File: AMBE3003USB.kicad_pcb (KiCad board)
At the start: 2 copper layers, 95 x 85 mm, 208 parts, among them J1 McBSP, J2 USB_OTG, J4 CODEC, P1 GND, P2 Config, P3 3v3, P4 VSET, P5 HARD RESET, P6 SEQ, P7 3v3, P8 ACONF, P9 GND, Q1 BC847, U1 AMBE3003, U2 TPS75005RGW_wPin21, U3 FT232RL, X1 29.4912

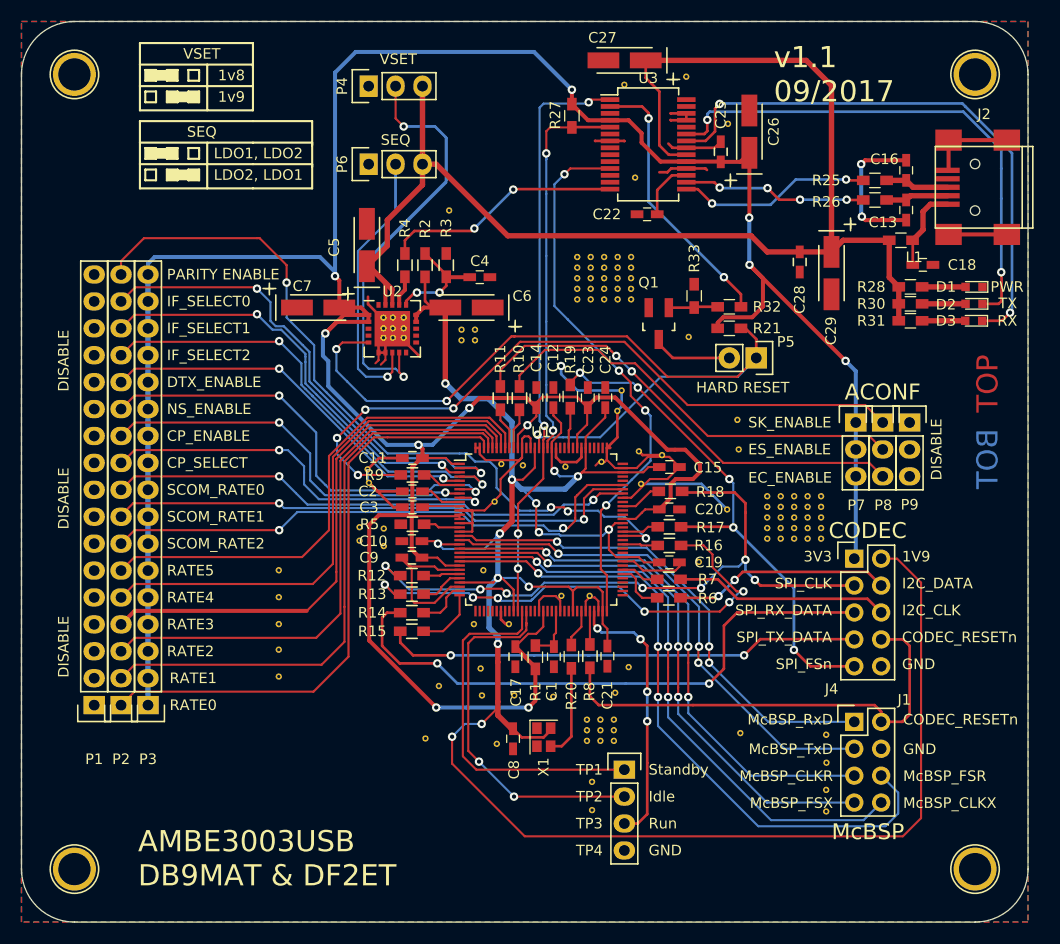
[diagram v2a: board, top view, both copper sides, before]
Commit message: Refactor labels
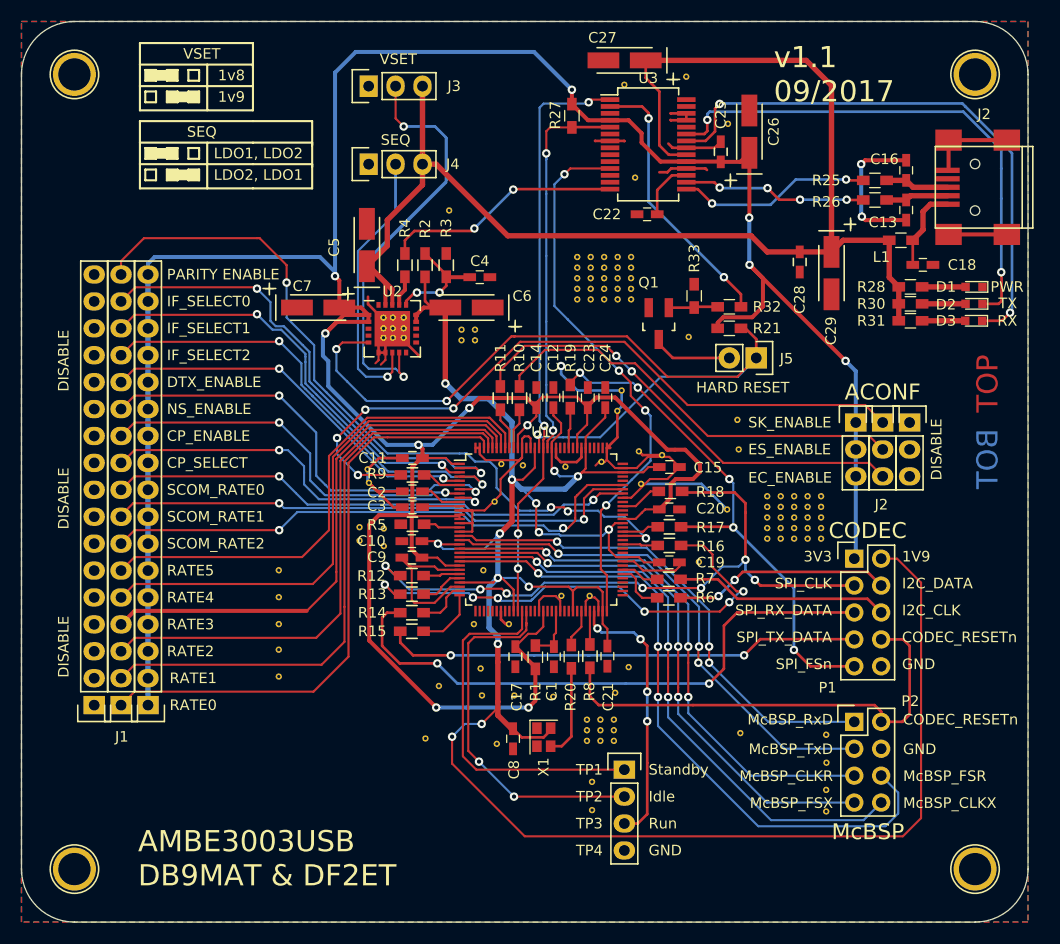
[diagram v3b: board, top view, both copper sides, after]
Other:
- board text added: "J1"
- board text added: "J2"
- board text added: "J3"
- board text added: "J4"
- board text added: "J5"
- board text added: "P1"
- board text added: "P2"
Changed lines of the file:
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@@
     (area 31.974499 47.974499 127.025501 133.025501)
     (thickness 1.6)
-    (drawings 152)
+    (drawings 159)
     (tracks 1325)
     (zones 0)
@@
   )
   (setup
-    (last_trace_width 0.2)
+    (last_trace_width 0.25)
     (user_trace_width 0.2)
     (user_trace_width 0.254)
@@
     (pad_to_mask_clearance 0.2)
     (aux_axis_origin 0 0)
-    (visible_elements 7FFFFFDF)
+    (visible_elements 7FFFFF7F)
     (pcbplotparams
       (layerselection 0x010fc_80000001)
@@
     (descr "Through hole pin header")
     (tags "pin header")
-    (fp_text reference J1 (at 4.716 -2.086) (layer F.SilkS)
+    (fp_text reference J1 (at 4.716 -2.086) (layer F.SilkS) hide
       (effects (font (size 1 1) (thickness 0.15)))
     )
@@
     (tags "capacitor 0603")
     (attr smd)
-    (fp_text reference C2 (at 4.2 0 180) (layer F.SilkS)
+    (fp_text reference C2 (at 3.368 -0.106 180) (layer F.SilkS)
       (effects (font (size 1 1) (thickness 0.15)))
     )
@@
     (tags "capacitor 0603")
     (attr smd)
-    (fp_text reference C3 (at 4.1 0 180) (layer F.SilkS)
+    (fp_text reference C3 (at 3.368 0.124 180) (layer F.SilkS)
       (effects (font (size 1 1) (thickness 0.15)))
     )
@@
     (tags "capacitor 0603")
     (attr smd)
-    (fp_text reference C10 (at 3.65 0 180) (layer F.SilkS)
+    (fp_text reference C10 (at 3.826 0.022 180) (layer F.SilkS)
       (effects (font (size 1 1) (thickness 0.15)))
     )
@@
     (tags "capacitor 0603")
     (attr smd)
-    (fp_text reference C19 (at 3.7 0) (layer F.SilkS)
+    (fp_text reference C19 (at 3.878 0.01) (layer F.SilkS)
       (effects (font (size 1 1) (thickness 0.15)))
     )
@@
     (tags "capacitor 0603")
     (attr smd)
-    (fp_text reference C20 (at 3.75 0) (layer F.SilkS)
+    (fp_text reference C20 (at 3.878 -0.07) (layer F.SilkS)
       (effects (font (size 1 1) (thickness 0.15)))
     )
@@
     (tags "capacitor 0603")
     (attr smd)
-    (fp_text reference C21 (at 3.7 0 270) (layer F.SilkS)
+    (fp_text reference C21 (at 3.86 -0.076 270) (layer F.SilkS)
       (effects (font (size 1 1) (thickness 0.15)))
     )
@@
     (tags "capacitor 0603")
     (attr smd)
-    (fp_text reference C23 (at 3.55 0.05 90) (layer F.SilkS)
+    (fp_text reference C23 (at 3.744 0.148 90) (layer F.SilkS)
       (effects (font (size 1 1) (thickness 0.15)))
     )
@@
     (tags "capacitor 0603")
     (attr smd)
-    (fp_text reference C24 (at 3.575 0.025 90) (layer F.SilkS)
+    (fp_text reference C24 (at 3.744 0.022 90) (layer F.SilkS)
       (effects (font (size 1 1) (thickness 0.15)))
     )
@@
     (tags "resistor 0603")
     (attr smd)
-    (fp_text reference L1 (at -1.25 -1.6 180) (layer F.SilkS)
+    (fp_text reference L1 (at 1.843 -1.581 180) (layer F.SilkS)
       (effects (font (size 1 1) (thickness 0.15)))
     )
@@
     (tags "resistor 0603")
     (attr smd)
-    (fp_text reference R19 (at -3.5 0 270) (layer F.SilkS)
+    (fp_text reference R19 (at -3.644 -0.02 270) (layer F.SilkS)
       (effects (font (size 1 1) (thickness 0.15)))
     )
@@
     (tags "resistor 0603")
     (attr smd)
-    (fp_text reference R20 (at -3.7 0 90) (layer F.SilkS)
+    (fp_text reference R20 (at -3.81 -0.08 90) (layer F.SilkS)
       (effects (font (size 1 1) (thickness 0.15)))
     )
@@
     (descr "Through hole pin header")
     (tags "pin header")
-    (fp_text reference P4 (at 0 -2.5 90) (layer F.SilkS)
+    (fp_text reference P4 (at 0 -2.794 180) (layer F.SilkS) hide
       (effects (font (size 1 1) (thickness 0.15)))
     )
@@
     (tags "resistor 0603")
     (attr smd)
-    (fp_text reference R5 (at -4.05 0) (layer F.SilkS)
+    (fp_text reference R5 (at -3.368 0.054) (layer F.SilkS)
       (effects (font (size 1 1) (thickness 0.15)))
     )
@@
     (tags "resistor 0603")
     (attr smd)
-    (fp_text reference R6 (at -3.65 -0.05 180) (layer F.SilkS)
+    (fp_text reference R6 (at -3.42 0.038 180) (layer F.SilkS)
       (effects (font (size 1 1) (thickness 0.15)))
     )
@@
     (tags "resistor 0603")
     (attr smd)
-    (fp_text reference R7 (at -3.65 0 180) (layer F.SilkS)
+    (fp_text reference R7 (at -3.42 0.066 180) (layer F.SilkS)
       (effects (font (size 1 1) (thickness 0.15)))
     )
@@
     (tags "resistor 0603")
     (attr smd)
-    (fp_text reference R9 (at -3.6 0) (layer F.SilkS)
+    (fp_text reference R9 (at -3.368 -0.122) (layer F.SilkS)
       (effects (font (size 1 1) (thickness 0.15)))
     )
@@
     (tags "resistor 0603")
     (attr smd)
-    (fp_text reference R10 (at -3.7 0.05 270) (layer F.SilkS)
+    (fp_text reference R10 (at -3.794 0.006 270) (layer F.SilkS)
       (effects (font (size 1 1) (thickness 0.15)))
     )
@@
     (tags "resistor 0603")
     (attr smd)
-    (fp_text reference R11 (at -3.7 0 270) (layer F.SilkS)
+    (fp_text reference R11 (at -3.794 -0.016 270) (layer F.SilkS)
       (effects (font (size 1 1) (thickness 0.15)))
     )
@@
     (tags "resistor 0603")
     (attr smd)
-    (fp_text reference R12 (at -3.8 0) (layer F.SilkS)
+    (fp_text reference R12 (at -3.826 0.03) (layer F.SilkS)
       (effects (font (size 1 1) (thickness 0.15)))
     )
@@
     (tags "resistor 0603")
     (attr smd)
-    (fp_text reference R16 (at -3.7 0 180) (layer F.SilkS)
+    (fp_text reference R16 (at -3.878 -0.086 180) (layer F.SilkS)
       (effects (font (size 1 1) (thickness 0.15)))
     )
@@
     (descr "Through hole pin header")
     (tags "pin header")
-    (fp_text reference P5 (at -1.524 -2.794 360) (layer F.SilkS)
+    (fp_text reference P5 (at -0.762 -2.794 360) (layer F.SilkS) hide
       (effects (font (size 1 1) (thickness 0.15)))
     )
@@
     (descr "Through hole pin header")
     (tags "pin header")
-    (fp_text reference P6 (at 0 -2.5 90) (layer F.SilkS)
+    (fp_text reference P6 (at 0 -2.794 180) (layer F.SilkS) hide
       (effects (font (size 1 1) (thickness 0.15)))
     )
@@
     (tags "capacitor 0603")
     (attr smd)
-    (fp_text reference C9 (at 4.05 0 180) (layer F.SilkS)
+    (fp_text reference C9 (at 3.318 0.048 180) (layer F.SilkS)
       (effects (font (size 1 1) (thickness 0.15)))
     )
@@
     (tags "capacitor 0603")
     (attr smd)
-    (fp_text reference C17 (at 3.3655 -0.0635 450) (layer F.SilkS)
+    (fp_text reference C17 (at 3.81 -0.127 450) (layer F.SilkS)
       (effects (font (size 1 1) (thickness 0.15)))
     )
@@
     (descr "Through hole pin header")
     (tags "pin header")
-    (fp_text reference J4 (at -2.142 12.298) (layer F.SilkS)
+    (fp_text reference J4 (at -2.65 12.044) (layer F.SilkS) hide
       (effects (font (size 1 1) (thickness 0.15)))
     )
@@
     (descr "Through hole pin header")
     (tags "pin header")
-    (fp_text reference P7 (at 0.05 7.8) (layer F.SilkS)
+    (fp_text reference P7 (at 0.05 7.8) (layer F.SilkS) hide
       (effects (font (size 1 1) (thickness 0.15)))
     )
@@
     (descr "Through hole pin header")
     (tags "pin header")
-    (fp_text reference P8 (at 0.05 7.8) (layer F.SilkS)
+    (fp_text reference P8 (at 0.05 7.8) (layer F.SilkS) hide
       (effects (font (size 1 1) (thickness 0.15)))
     )
@@
     (descr "Through hole pin header")
     (tags "pin header")
-    (fp_text reference P9 (at 0 7.75) (layer F.SilkS)
+    (fp_text reference P9 (at 0 7.75) (layer F.SilkS) hide
       (effects (font (size 1 1) (thickness 0.15)))
     )
@@
     (descr "Through hole pin header")
     (tags "pin header")
-    (fp_text reference P1 (at 0 -5.1 180) (layer F.SilkS)
+    (fp_text reference P1 (at 0 -2.54 180) (layer F.SilkS) hide
       (effects (font (size 1 1) (thickness 0.15)))
     )
-    (fp_text value GND (at 0 -3.1 180) (layer F.Fab)
+    (fp_text value GND (at 3.81 0 180) (layer F.Fab)
       (effects (font (size 1 1) (thickness 0.15)))
     )
@@
     (descr "Through hole pin header")
     (tags "pin header")
-    (fp_text reference P2 (at 0 -5.1 180) (layer F.SilkS)
+    (fp_text reference P2 (at 0 -2.54 180) (layer F.SilkS) hide
       (effects (font (size 1 1) (thickness 0.15)))
     )
-    (fp_text value Config (at 0 -3.1 180) (layer F.Fab)
+    (fp_text value Config (at 0 -5.334 180) (layer F.Fab)
       (effects (font (size 1 1) (thickness 0.15)))
     )
@@
     (descr "Through hole pin header")
     (tags "pin header")
-    (fp_text reference P3 (at 0 -5.1 180) (layer F.SilkS)
+    (fp_text reference P3 (at 0 -2.54 180) (layer F.SilkS) hide
       (effects (font (size 1 1) (thickness 0.15)))
     )
-    (fp_text value 3v3 (at 0 -3.1 180) (layer F.Fab)
+    (fp_text value 3v3 (at -3.81 -1.778 180) (layer F.Fab)
       (effects (font (size 1 1) (thickness 0.15)))
     )
@@
     )
   )
+  (gr_text P2 (at 115.8875 112.141) (layer F.SilkS)
+    (effects (font (size 1 1) (thickness 0.15)))
+  )
+  (gr_text P1 (at 108.077 110.871) (layer F.SilkS)
+    (effects (font (size 1 1) (thickness 0.15)))
+  )
+  (gr_text J1 (at 41.4655 115.5065) (layer F.SilkS)
+    (effects (font (size 1 1) (thickness 0.15)))
+  )
+  (gr_text J5 (at 104.2035 79.8195) (layer F.SilkS)
+    (effects (font (size 1 1) (thickness 0.15)))
+  )
+  (gr_text J4 (at 72.7075 61.468) (layer F.SilkS)
+    (effects (font (size 1 1) (thickness 0.15)))
+  )
+  (gr_text J3 (at 72.8345 54.102) (layer F.SilkS)
+    (effects (font (size 1 1) (thickness 0.15)))
+  )
+  (gr_text J2 (at 113.157 93.599) (layer F.SilkS)
+    (effects (font (size 1 1) (thickness 0.15)))
+  )
   (gr_text "PARITY ENABLE" (at 45.72 71.882) (layer F.SilkS)

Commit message: Add nice logo
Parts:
- added OSHW_COPPER_10MM: VAL**, Symbols:OSHW_COPPER_10MM, F.Cu at (64.3, 115.8)
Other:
- board text added: "hardware"
- board text added: "open source"
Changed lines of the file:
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@@
     (links 392)
     (no_connects 0)
-    (area 31.974499 47.974499 127.025501 133.025501)
+    (area 31.974499 41.5 138.65 133.025501)
     (thickness 1.6)
-    (drawings 159)
+    (drawings 161)
     (tracks 1325)
     (zones 0)
-    (modules 208)
+    (modules 209)
     (nets 85)
   )
@@
       (drillshape 0)
       (scaleselection 1)
-      (outputdirectory /opt/AMBE3003USB/))
+      (outputdirectory /opt/AMBE3003USB/gerbers/))
   )
   (net 0 "")
@@
     )
   )
+  (module Symbols:OSHW_COPPER_10MM (layer F.Cu)
+    (at 64.262 115.824)
+    (fp_text reference OSHW_COPPER_10MM (at 0 5.461) (layer F.SilkS) hide
+      (effects (font (thickness 0.3048)))
+    )
+    (fp_text value VAL** (at 0 -7.239) (layer F.SilkS) hide
+      (effects (font (thickness 0.3048)))
+    )
+    (pad "" smd trapezoid (at 0 -4.1656 180) (size 1.45796 1.4986) (rect_delta 0 -0.2794 ) (layers F.Cu F.Paste F.Mask))
+    (pad "" smd trapezoid (at 2.94386 -2.94386 135) (size 1.45796 1.4986) (rect_delta 0 -0.2794 ) (layers F.Cu F.Paste F.Mask))
+    (pad "" smd trapezoid (at 4.1656 0 90) (size 1.45796 1.4986) (rect_delta 0 -0.2794 ) (layers F.Cu F.Paste F.Mask))
+    (pad "" smd trapezoid (at 2.94386 2.94386 45) (size 1.45796 1.4986) (rect_delta 0 -0.2794 ) (layers F.Cu F.Paste F.Mask))
+    (pad "" smd trapezoid (at -2.94386 -2.94386 225) (size 1.45796 1.4986) (rect_delta 0 -0.2794 ) (layers F.Cu F.Paste F.Mask))
+    (pad "" smd trapezoid (at -4.1656 0 270) (size 1.45796 1.4986) (rect_delta 0 -0.2794 ) (layers F.Cu F.Paste F.Mask))
+    (pad "" smd trapezoid (at -2.94386 2.94386 315) (size 1.45796 1.4986) (rect_delta 0 -0.2794 ) (layers F.Cu F.Paste F.Mask))
+    (pad "" smd trapezoid (at 0 -2.39522 180) (size 1.08204 2.29108) (rect_delta 0 0.41402 ) (layers F.Cu F.Paste F.Mask))
+    (pad "" smd trapezoid (at -0.9144 -2.21234 202.5) (size 1.08204 2.29108) (rect_delta 0 0.41402 ) (layers F.Cu F.Paste F.Mask))
+    (pad "" smd trapezoid (at 0.9144 -2.21234 157.5) (size 1.08204 2.29108) (rect_delta 0 0.41402 ) (layers F.Cu F.Paste F.Mask))
+    (pad "" smd trapezoid (at 1.69164 -1.69164 135) (size 1.08204 2.29108) (rect_delta 0 0.41402 ) (layers F.Cu F.Paste F.Mask))
+    (pad "" smd trapezoid (at -1.69164 -1.69164 225) (size 1.08204 2.29108) (rect_delta 0 0.41402 ) (layers F.Cu F.Paste F.Mask))
+    (pad "" smd trapezoid (at 2.21234 -0.9144 112.5) (size 1.08204 2.29108) (rect_delta 0 0.41402 ) (layers F.Cu F.Paste F.Mask))
+    (pad "" smd trapezoid (at -2.21234 -0.9144 247.5) (size 1.08204 2.29108) (rect_delta 0 0.41402 ) (layers F.Cu F.Paste F.Mask))
+    (pad "" smd trapezoid (at 2.39522 0 90) (size 1.08204 2.29108) (rect_delta 0 0.41402 ) (layers F.Cu F.Paste F.Mask))
+    (pad "" smd trapezoid (at -2.39522 0 270) (size 1.08204 2.29108) (rect_delta 0 0.41402 ) (layers F.Cu F.Paste F.Mask))
+    (pad "" smd trapezoid (at -2.21234 0.9144 292.5) (size 1.08204 2.29108) (rect_delta 0 0.41402 ) (layers F.Cu F.Paste F.Mask))
+    (pad "" smd trapezoid (at 2.21234 0.9144 67.5) (size 1.08204 2.29108) (rect_delta 0 0.41402 ) (layers F.Cu F.Paste F.Mask))
+    (pad "" smd trapezoid (at 1.69164 1.69164 45) (size 1.08204 2.29108) (rect_delta 0 0.41402 ) (layers F.Cu F.Paste F.Mask))
+    (pad "" smd trapezoid (at -1.69164 1.69164 315) (size 1.08204 2.29108) (rect_delta 0 0.41402 ) (layers F.Cu F.Paste F.Mask))
+    (pad "" smd trapezoid (at -1.32842 1.99136 326.3) (size 0.54102 2.29108) (rect_delta 0 0.20828 ) (layers F.Cu F.Paste F.Mask))
+    (pad "" smd trapezoid (at 1.32842 1.99136 33.7) (size 0.54102 2.29108) (rect_delta 0 0.20828 ) (layers F.Cu F.Paste F.Mask))
+  )
+  (gr_text hardware (at 63.7286 122.7074) (layer F.SilkS)
+    (effects (font (size 1.5 1.5) (thickness 0.3)))
+  )
+  (gr_text "open source" (at 64.262 120.904) (layer F.SilkS)
+    (effects (font (size 1.5 1.5) (thickness 0.3)))
+  )
   (gr_text P2 (at 115.8875 112.141) (layer F.SilkS)
     (effects (font (size 1 1) (thickness 0.15)))
@@
     (effects (font (size 1 1) (thickness 0.15)))
   )
-  (gr_text "AMBE3003USB\nDB9MAT & DF2ET" (at 43 127) (layer F.SilkS)
+  (gr_text "AMBE3003USB\nDB9MAT & DF2ET" (at 42.1005 128.4605) (layer F.SilkS)
     (effects (font (size 2 2) (thickness 0.5)) (justify left))
   )

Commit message: Correct polarisation for C6 and C7
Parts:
- turned C6 to 0 degrees
- turned C7 to 180 degrees
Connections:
- C6 pad 1: GND -> +1V9
- C6 pad 2: +1V9 -> GND
- C7 pad 1: GND -> +3V3
- C7 pad 2: +3V3 -> GND
- J2 pad 4: (no net) -> Net-(J2-Pad4)
- U1 pad 100: (no net) -> Net-(U1-Pad100)
- U1 pad 101: (no net) -> Net-(U1-Pad101)
- U1 pad 105: (no net) -> Net-(U1-Pad105)
- U1 pad 107: (no net) -> Net-(U1-Pad107)
- U1 pad 108: (no net) -> Net-(U1-Pad108)
- U1 pad 116: (no net) -> Net-(U1-Pad116)
- U1 pad 33: (no net) -> Net-(U1-Pad33)
- U1 pad 34: (no net) -> Net-(U1-Pad34)
- U1 pad 35: (no net) -> Net-(U1-Pad35)
- U1 pad 36: (no net) -> Net-(U1-Pad36)
- U1 pad 37: (no net) -> Net-(U1-Pad37)
- U1 pad 38: (no net) -> Net-(U1-Pad38)
- U1 pad 40: (no net) -> Net-(U1-Pad40)
- U1 pad 41: (no net) -> Net-(U1-Pad41)
- U1 pad 46: (no net) -> Net-(U1-Pad46)
- U1 pad 47: (no net) -> Net-(U1-Pad47)
- U1 pad 50: (no net) -> Net-(U1-Pad50)
- U1 pad 51: (no net) -> Net-(U1-Pad51)
- U1 pad 54: (no net) -> Net-(U1-Pad54)
- U1 pad 55: (no net) -> Net-(U1-Pad55)
- U1 pad 57: (no net) -> Net-(U1-Pad57)
- U1 pad 65: (no net) -> Net-(U1-Pad65)
- U1 pad 66: (no net) -> Net-(U1-Pad66)
- U1 pad 67: (no net) -> Net-(U1-Pad67)
- U1 pad 68: (no net) -> Net-(U1-Pad68)
- U1 pad 69: (no net) -> Net-(U1-Pad69)
- U1 pad 72: (no net) -> Net-(U1-Pad72)
- U1 pad 75: (no net) -> Net-(U1-Pad75)
- U1 pad 76: (no net) -> Net-(U1-Pad76)
- U1 pad 78: (no net) -> Net-(U1-Pad78)
- U1 pad 81: (no net) -> Net-(U1-Pad81)
- U1 pad 84: (no net) -> Net-(U1-Pad84)
- U1 pad 85: (no net) -> Net-(U1-Pad85)
- U1 pad 87: (no net) -> Net-(U1-Pad87)
- U1 pad 92: (no net) -> Net-(U1-Pad92)
- U1 pad 93: (no net) -> Net-(U1-Pad93)
- U1 pad 96: (no net) -> Net-(U1-Pad96)
- U1 pad 98: (no net) -> Net-(U1-Pad98)
- U1 pad 99: (no net) -> Net-(U1-Pad99)
- U2 pad 10: (no net) -> Net-(U2-Pad10)
- U2 pad 11: (no net) -> Net-(U2-Pad11)
- U2 pad 12: (no net) -> Net-(U2-Pad12)
- U2 pad 13: (no net) -> Net-(U2-Pad13)
- U2 pad 20: (no net) -> Net-(U2-Pad20)
- U2 pad 3: (no net) -> Net-(U2-Pad3)
- U2 pad 4: (no net) -> Net-(U2-Pad4)
- U3 pad 10: (no net) -> Net-(U3-Pad10)
- U3 pad 12: (no net) -> Net-(U3-Pad12)
- U3 pad 13: (no net) -> Net-(U3-Pad13)
- U3 pad 27: (no net) -> Net-(U3-Pad27)
- U3 pad 28: (no net) -> Net-(U3-Pad28)
- U3 pad 3: (no net) -> Net-(U3-Pad3)
- U3 pad 6: (no net) -> Net-(U3-Pad6)
- U3 pad 9: (no net) -> Net-(U3-Pad9)
- X1 pad 1: (no net) -> Net-(X1-Pad1)
